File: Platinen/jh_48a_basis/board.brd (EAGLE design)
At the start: 23.3 x 21 mm, 29 parts, among them X1 14867

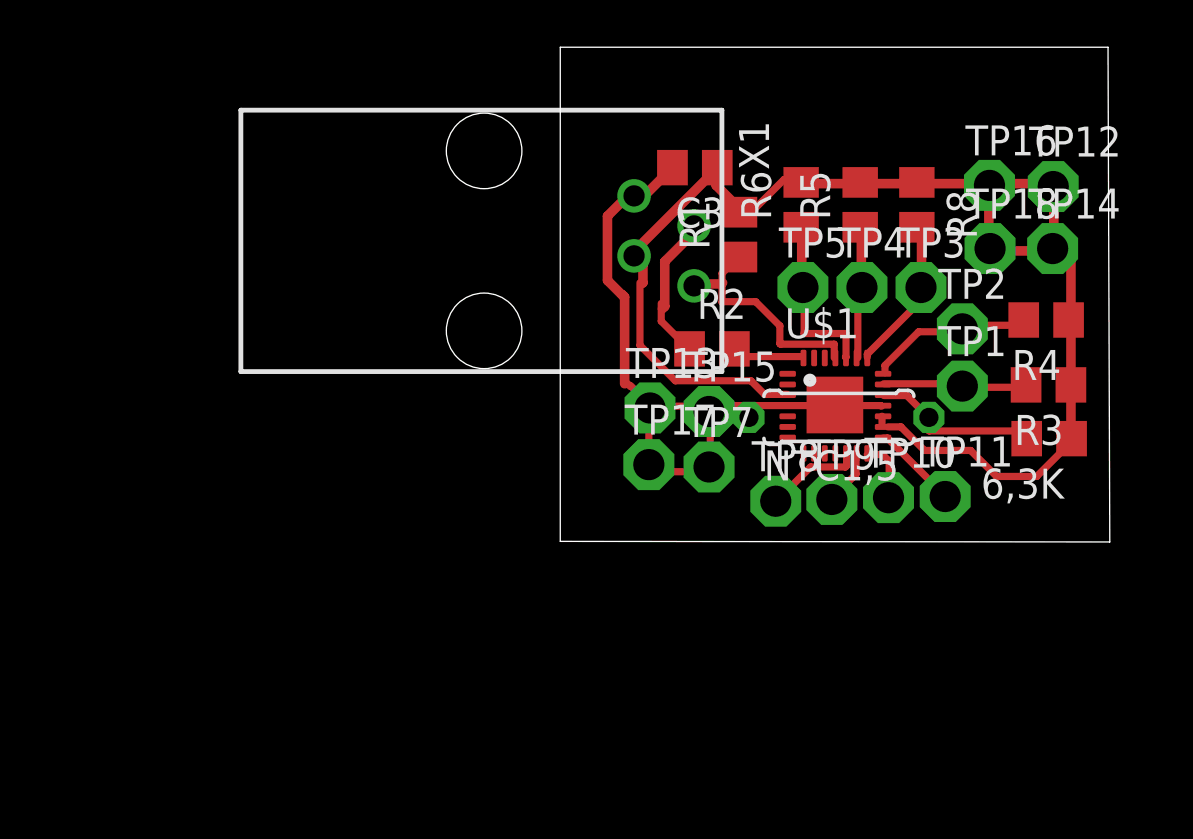
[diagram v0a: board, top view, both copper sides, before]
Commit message: layout: update with C
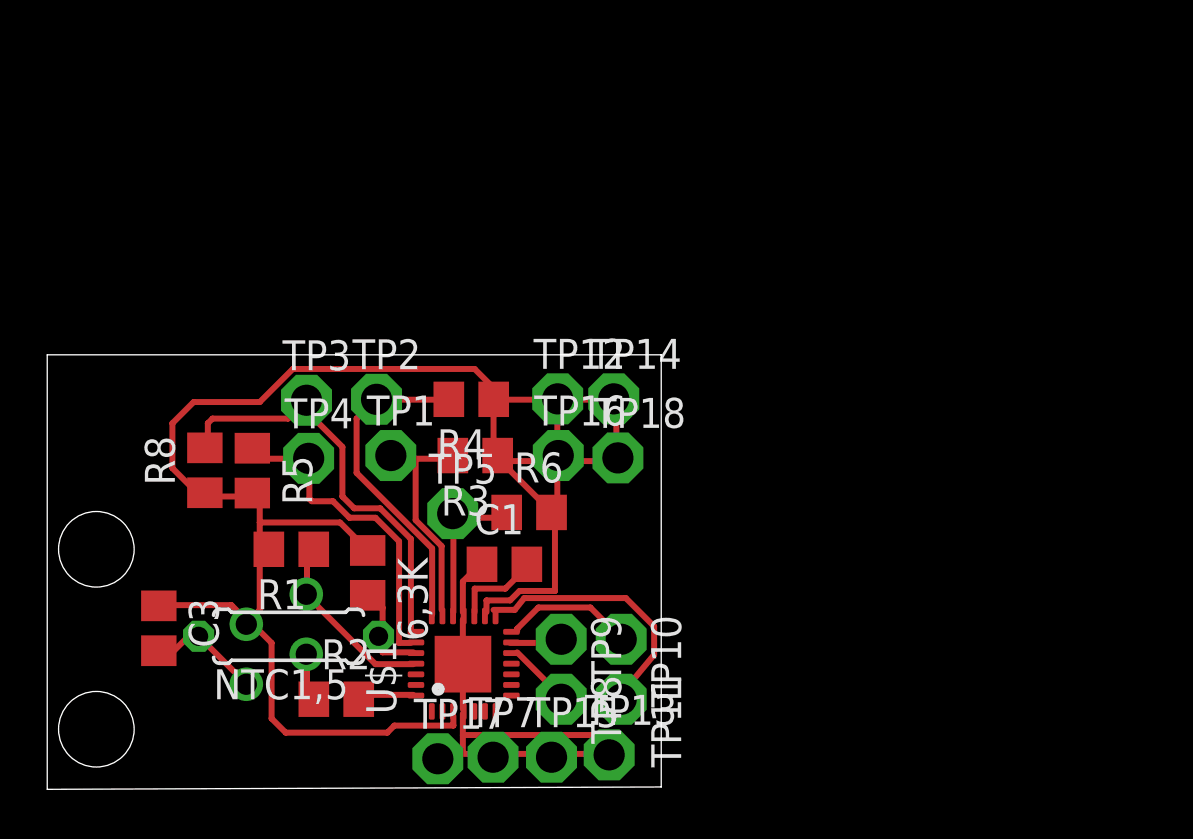
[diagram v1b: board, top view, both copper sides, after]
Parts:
- added C1: (no value), rcl:C0805
- moved R8 32.2 mm to (6.67, 13.5), turned to 90 degrees
- moved C3 29.9 mm to (4.72, 6.82), turned to 270 degrees
- moved 6,3K 29.4 mm to (13.6, 9.16), turned to 270 degrees
- moved R5 28.1 mm to (8.69, 13.5), turned to 270 degrees
- moved TP3 26.5 mm to (11.0, 16.5)
- moved NTC1,5 25.1 mm to (10.2, 6.48)
- moved TP2 25.0 mm to (13.9, 16.5)
- moved R4 24.6 mm to (18.0, 16.5)
- moved TP4 24.5 mm to (11.1, 14.0)
- moved R3 24.5 mm to (18.1, 14.1)
- moved TP1 24.4 mm to (14.6, 14.1)
- moved X1 23.5 mm to (2.08, 6.36), flipped to the bottom, turned to 90 degrees
- moved R1 23.2 mm to (10.3, 10.2), turned to 180 degrees
- moved TP12 22.8 mm to (21.6, 16.5)
- moved R2 21.8 mm to (12.2, 3.81)
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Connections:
- removed net N$2: 6,3K.2, NTC1,5.1, U$1.19
- new net N$18: 6,3K.2, NTC1,5.1, U$1.24
- new net N$6: C1.2, U$1.17
- net GND: now also C1.1
- net N$17: now also U$1.19; no longer U$1.24
- net VCC: no longer U$1.17
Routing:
- net N$43: track 1.20 -> 18.7 mm
- net N$8: track 19.2 -> 2.10 mm
- net N$2: track 0.00 -> 11.0 mm
- net N$25: track 1.90 -> 12.7 mm
- net N$42: track 7.26 -> 16.7 mm
- net N$31: track 11.6 -> 2.15 mm
- net N$34: track 2.35 -> 11.3 mm
- net N$29: track 2.97 -> 10.8 mm
- net N$24: track 0.12 -> 7.54 mm
- net N$38: track 0.40 -> 7.20 mm
- net N$27: track 9.76 -> 4.10 mm
- net N$44: track 3.94 -> 0.00 mm
- net N$40: track 3.60 -> 7.50 mm
- net N$32: track 7.43 -> 3.57 mm
- net N$46: track 3.82 -> 0.00 mm
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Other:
- board size 23.3 x 21 mm -> 26 x 18.4 mm

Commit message: layout: update basis board
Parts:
- moved NTC1,5 0.31 mm to (10.1, 6.74)
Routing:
- net N$44: track 0.00 -> 11.0 mm
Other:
- board size 26 x 18.4 mm -> 26.2 x 18.4 mm
- board text added: "rev. A"

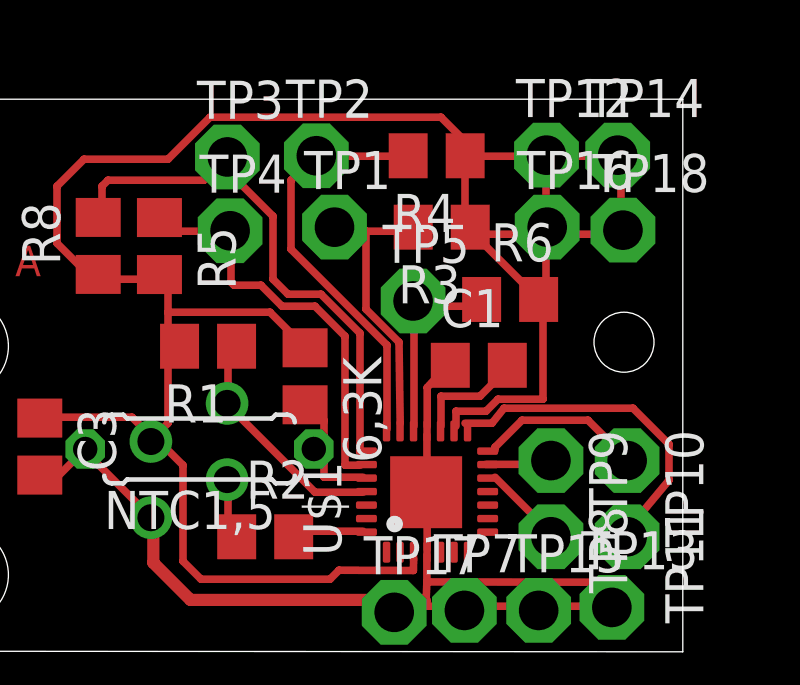
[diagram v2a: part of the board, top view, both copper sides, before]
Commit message: layout: made easier to produce
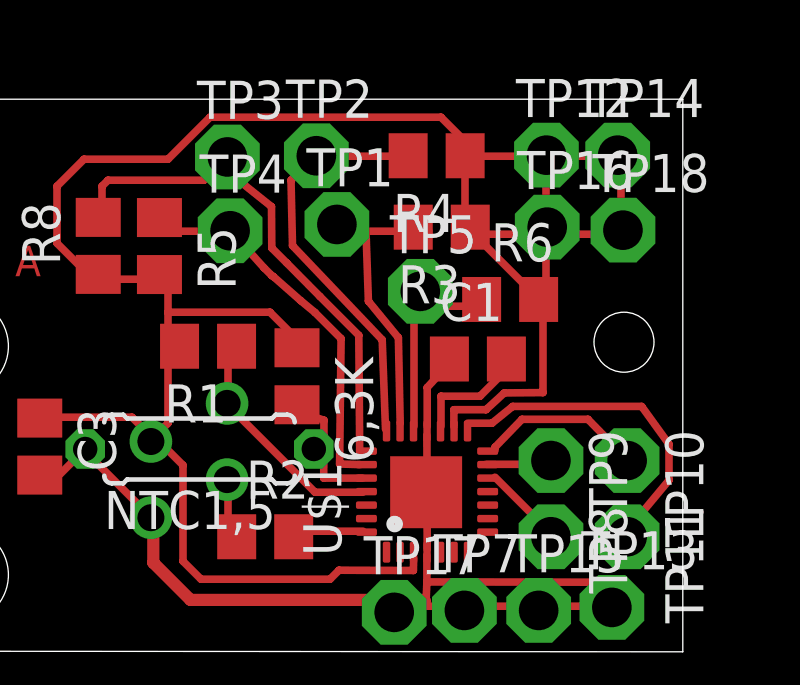
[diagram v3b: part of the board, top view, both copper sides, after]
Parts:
- moved TP5 0.40 mm to (17.4, 12.0)
- moved 6,3K 0.27 mm to (13.3, 9.16)
- moved C1 0.21 mm to (19.3, 9.74)
- moved TP1 0.12 mm to (14.6, 14.2)
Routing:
- net N$2: track 11.0 -> 10.00 mm
- net N$23: track 3.34 -> 4.18 mm
- net N$9: track 12.2 -> 11.6 mm
